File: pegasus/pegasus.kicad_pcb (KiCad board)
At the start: 2 copper layers, 39 x 98 mm, 22 parts, among them IC2 RFD900, IC3 L70B-M39, J1 Screw_Terminal_01x04, J2 Screw_Terminal_01x02, Q1 ST3413A, U1 Teensy4.0, U2 CON-SMA-EDGE-S, U3 CON-SMA-EDGE-S, U4 XTSD04GCLGEGA, U5 HT7350-A

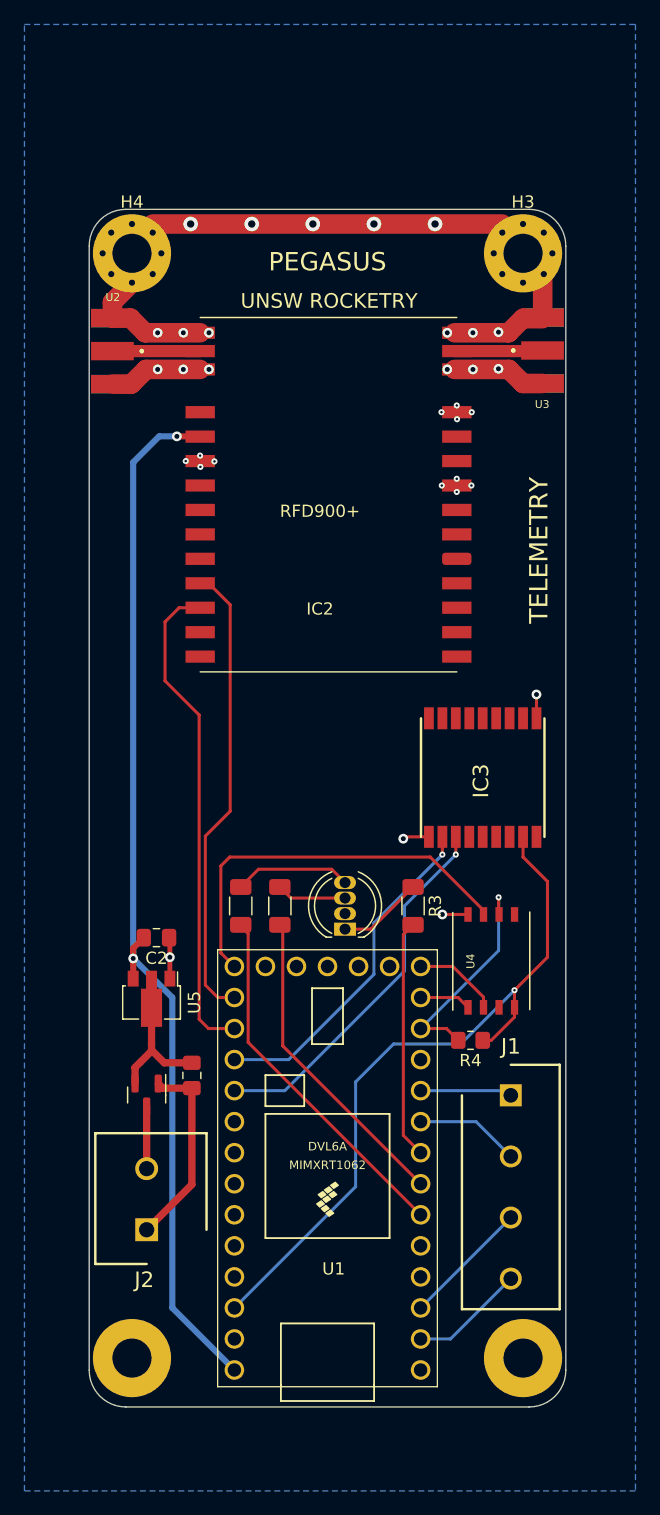
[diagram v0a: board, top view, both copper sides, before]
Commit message: add via stitching and more spacing between traces
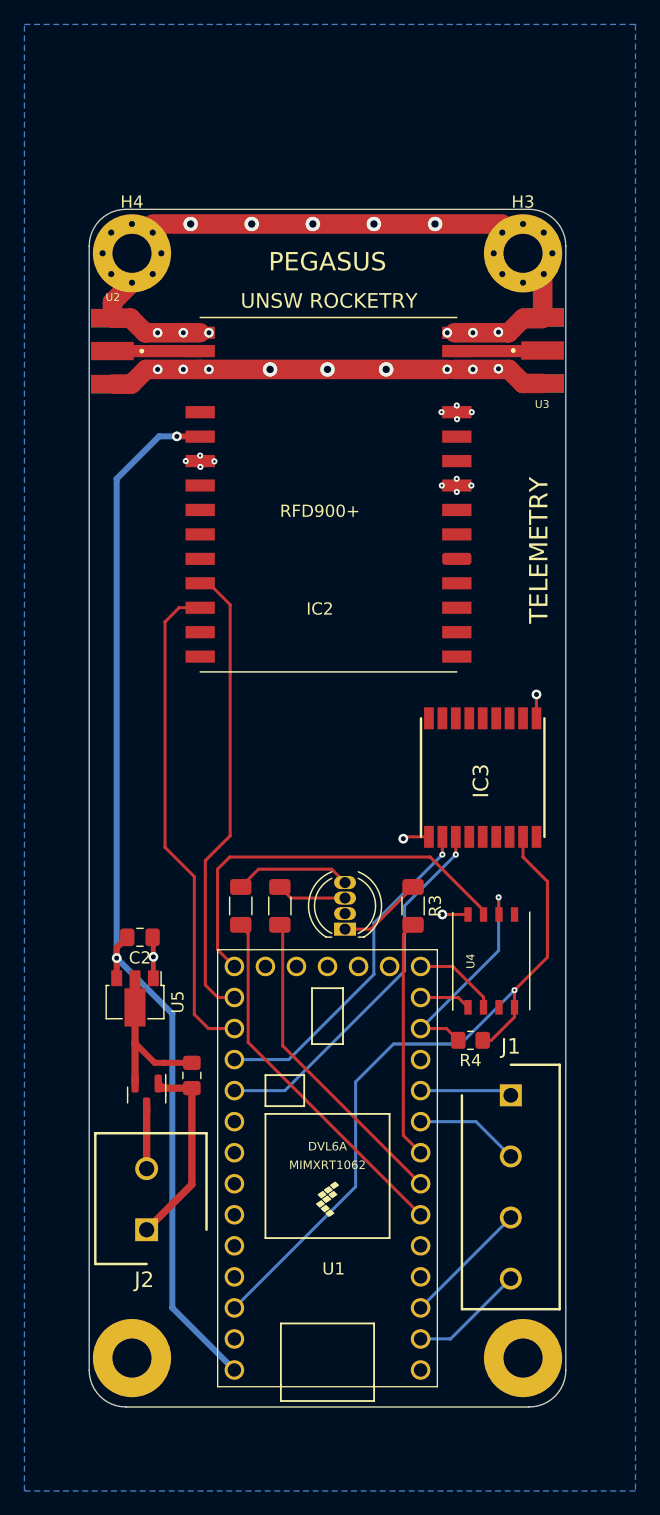
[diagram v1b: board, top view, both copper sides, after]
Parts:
- moved C2 1.35 mm to (90.2, 121.6)
- moved U5 1.35 mm to (89.8, 126.6)
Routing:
- net GND: track 94.5 -> 114.7 mm, vias 33 -> 36
- net +5V: track 87.9 -> 89.0 mm
- net Net-(C1-Pad2): track 12.8 -> 13.9 mm

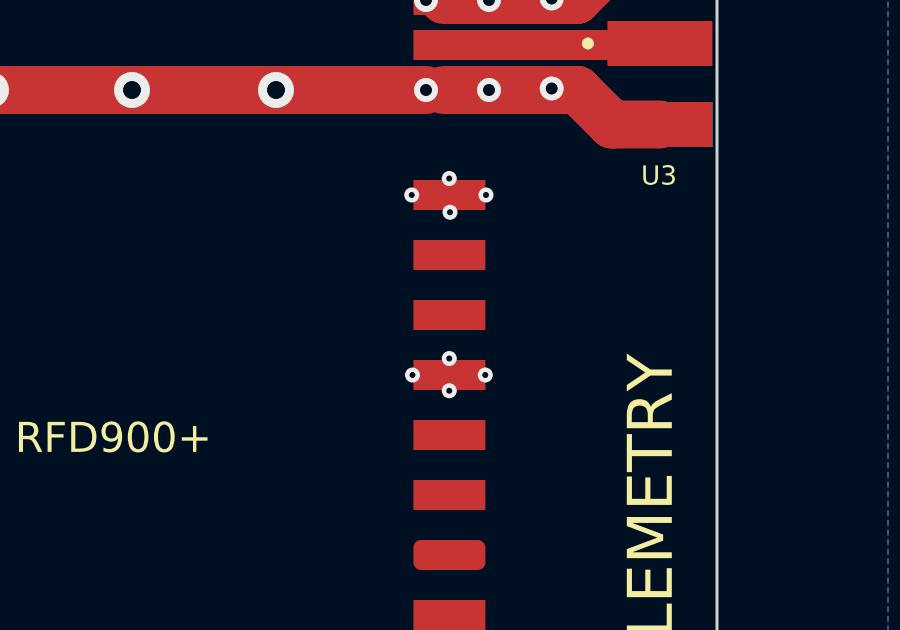
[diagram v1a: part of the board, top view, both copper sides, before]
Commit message: add missing round pin to rfd900
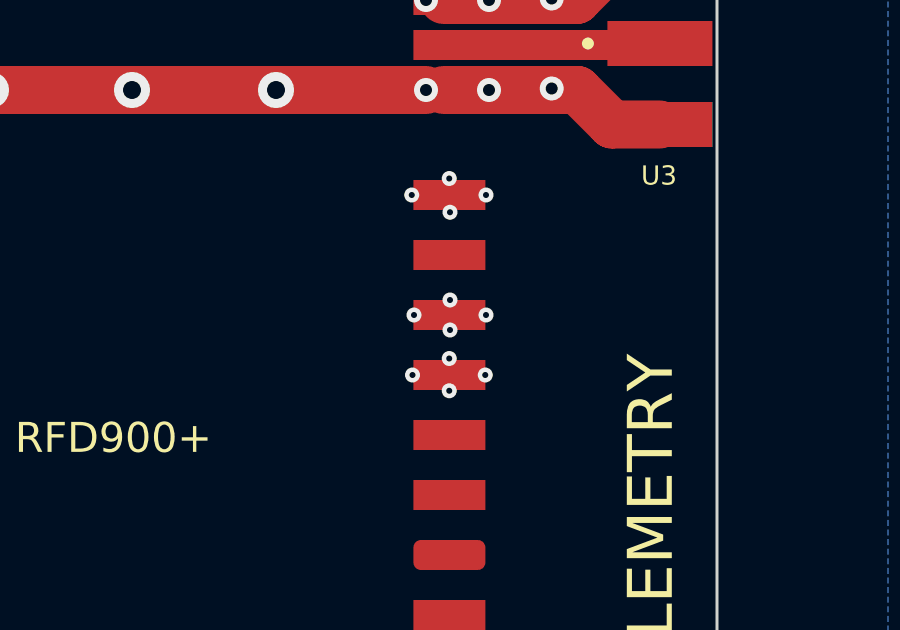
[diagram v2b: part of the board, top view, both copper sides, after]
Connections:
- IC2 pad 9: unconnected-(IC2-Pad9) -> GND
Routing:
- net GND: vias 36 -> 40

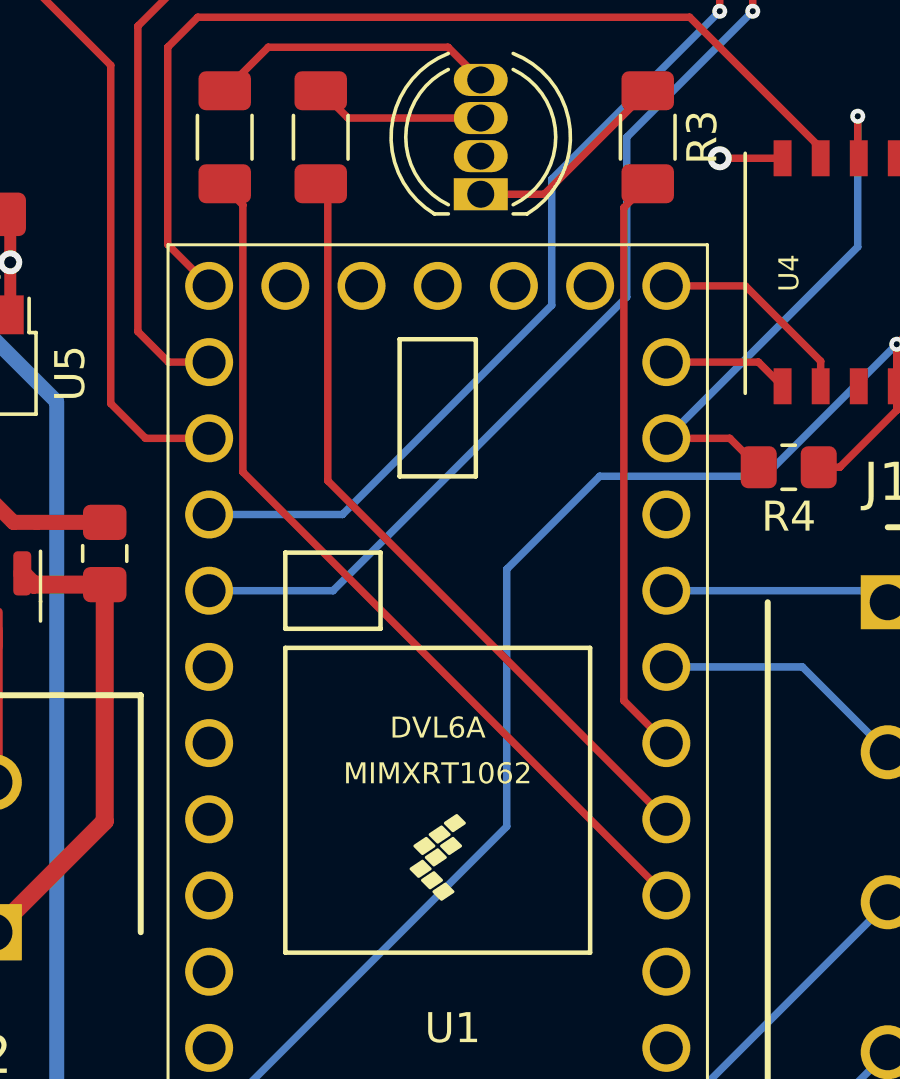
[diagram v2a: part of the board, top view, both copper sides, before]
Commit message: remove unused teensy 4 pins from footprint
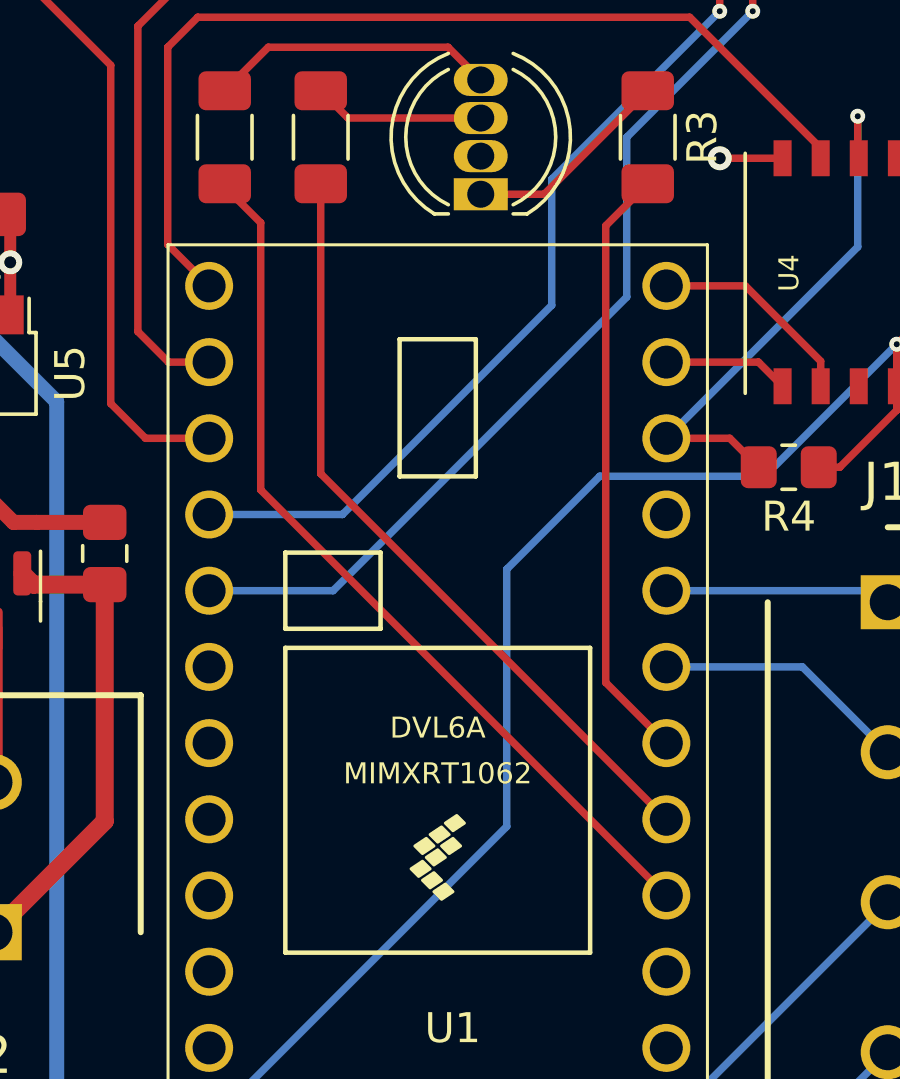
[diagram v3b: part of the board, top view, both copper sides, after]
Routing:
- net RGB3: track 19.6 -> 20.1 mm

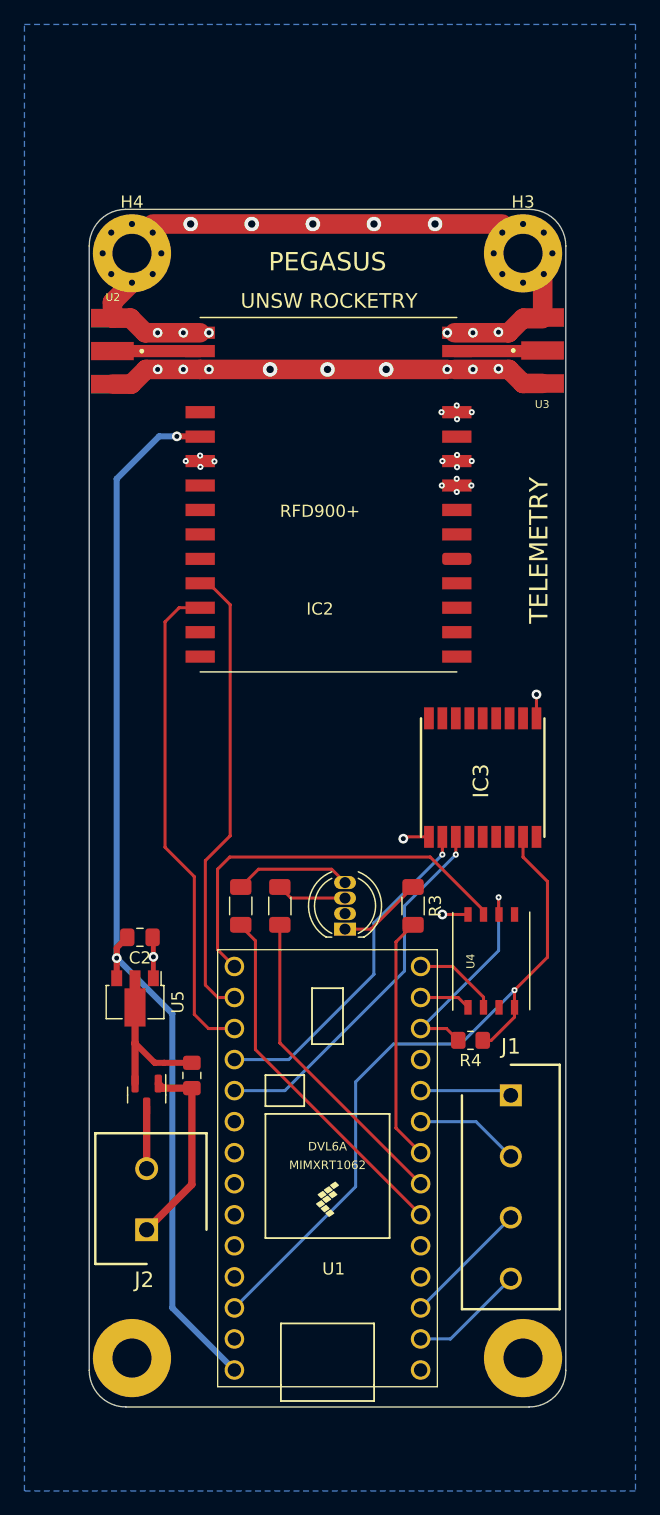
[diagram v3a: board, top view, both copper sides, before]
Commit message: replace voltage regulator with 1A capable, variable regulator. Increase via size for PCB mill prototyping. Add more vias for RFD900
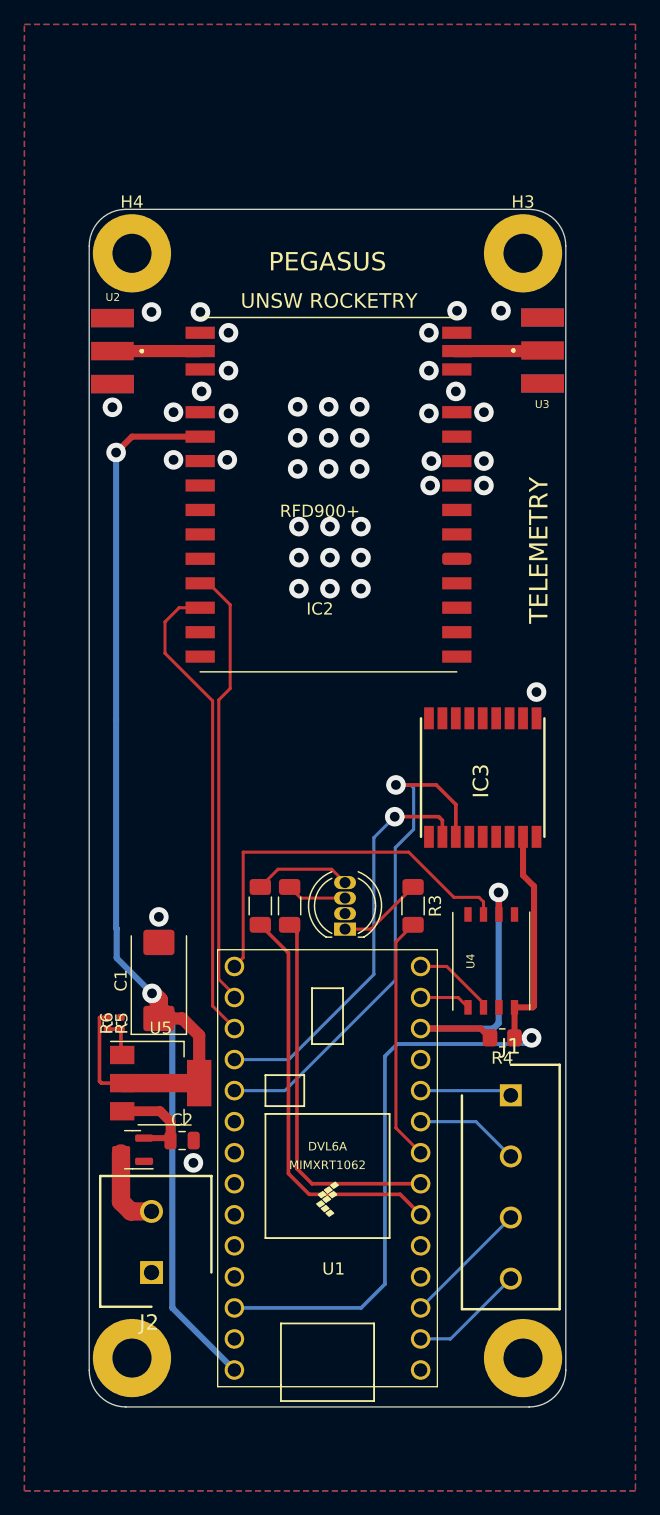
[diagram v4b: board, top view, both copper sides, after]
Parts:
- added R5: 50R, Capacitor_SMD:C_0402_1005Metric, F.Cu at (87.5, 128.6)
- added R6: 150R, Capacitor_SMD:C_0402_1005Metric, F.Cu at (88.6, 128.6)
- C1: value 1µF -> 22uF; footprint Capacitor_SMD:C_0805_2012Metric_Pad1.18x1.45mm_HandSolder -> Capacitor_Tantalum_SMD:CP_EIA-7343-30_AVX-N
- C2: value 1µF -> C; footprint Capacitor_SMD:C_0805_2012Metric_Pad1.18x1.45mm_HandSolder -> Capacitor_SMD:C_0805_2012Metric
- H3, H4: footprint MountingHole:MountingHole_3.2mm_M3_Pad_Via -> MountingHole:MountingHole_3.2mm_M3_Pad
- IC2: value RFD900 -> RFD900ux-SMT
- U5: value HT7350-A -> AZ1117-ADJ; footprint Package_TO_SOT_SMD:SOT-89-3 -> Package_TO_SOT_SMD:SOT-223-3_TabPin2
- moved C2 17.0 mm to (93.6, 138.2), turned to 0 degrees
- moved C1 8.23 mm to (91.7, 125.1)
- moved U5 7.24 mm to (91.8, 133.5), turned to 0 degrees
- moved Q1 4.62 mm to (89.5, 138.9), turned to 180 degrees
- moved J2 3.52 mm to (91.1, 149.0)
- moved R4 2.61 mm to (119.8, 129.8)
- moved R2 1.60 mm to (100.0, 119.0)
- moved R1 0.80 mm to (102.4, 119.0)
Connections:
- net /BATT+ renamed Net-(J2-Pad2)
- C1 pad 1: GND -> +5V
- C1 pad 2: Net-(C1-Pad2) -> GND
- C2 pad 1: GND -> Net-(Q1-Pad2)
- C2 pad 2: +5V -> GND
- IC2 pad 1: unconnected-(IC2-Pad1) -> VBUS
- IC2 pad 10: unconnected-(IC2-Pad10) -> +3V3
- IC2 pad 18: unconnected-(IC2-Pad18) -> GND
- IC3 pad 8: 3.3V -> +3V3
- Q1 pad 2: Net-(C1-Pad2) -> Net-(Q1-Pad2)
- R4 pad 1: 3.3V -> +3V3
- U1 pad 31: 3.3V -> +3V3
- U4 pad 8: 3.3V -> +3V3
- U5 pad 1: GND -> Net-(R5-Pad2)
- U5 pad 2: Net-(C1-Pad2) -> +5V
- U5 pad 3: +5V -> Net-(Q1-Pad2)
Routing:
- net GND: track 114.7 -> 2.27 mm, vias 40 -> 42
- net +3V3: track 0.00 -> 64.2 mm, vias 0 -> 1
- net 3.3V: track 58.8 -> 0.00 mm, vias 1 -> 0
- net +5V: track 89.0 -> 110.6 mm
- net Net-(C1-Pad2): track 13.9 -> 0.00 mm
- net TX4: track 30.7 -> 43.0 mm
- net Net-(Q1-Pad2): track 0.00 -> 8.10 mm
- net /CS: track 18.3 -> 25.1 mm
- net RX4: track 27.9 -> 33.3 mm
- net RGB2: track 26.0 -> 30.8 mm
- net RGB1: track 29.3 -> 33.5 mm
- net Net-(R5-Pad2): track 0.00 -> 3.26 mm
- net TX3: track 37.9 -> 36.2 mm
- net Net-(D1-Pad4): track 9.59 -> 7.99 mm
- net RX3: track 40.2 -> 39.0 mm
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- added copper zone on F.Cu, net GND
